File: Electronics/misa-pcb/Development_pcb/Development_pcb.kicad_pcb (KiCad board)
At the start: 2 copper layers, 100 x 100 mm, 25 parts, among them J1 Pan-Servo, J2 Tilt-Servo, J3 cam-power, J4 laser-power, J5 SPEAKER, J6 TFT_display, J7 lidar-TOF, J8 USB_C_IN, Q1 PN2222A, U1 ESP32-S3-DEVKITC-1-N8R8, U2 MP3-TF-16P

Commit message: Add new components and testing scripts for MISA PCB project
- Created MP3-TF-16P symbol library for KiCad with detailed properties.
- Added HTML redirect page for SnapEDA import guide.
- Implemented MISA_Camera_Only_Test.py for camera functionality testing with face detection.
- Developed TEST_1_PanTilt.ino for pan/tilt servo control with safety limits.
- Created TEST_2_DFPlayer.ino for standalone DFPlayer testing with serial control.
- Added TEST_3_Laser.ino for laser module testing with safety reminders.
- Implemented TEST_4_LiDAR.ino for TF-Luna LIDAR distance measurement.
- Developed TEST_5_TFT.ino for TFT screen testing with color fill and border checks.
- Added yolov8n.pt model file for object detection.
- Introduced Doctor and Human classes in Java with constructors and methods for specialization and name handling.
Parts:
- added C6: 100µF 16v, Capacitor_THT:CP_Radial_D5.0mm_P2.50mm, F.Cu at (254.0, 90.2)
- added G***: LOGO, LOGO, F.Cu at (255.3, 69.8)
- added G***: LOGO, LOGO, F.Cu at (266.1, 69.8)
- C1: renamed from C2; value 100nF -> 100nF 50v; footprint Capacitor_THT:C_Disc_D5.0mm_W2.5mm_P5.00mm -> Capacitor_THT:C_Disc_D5.0mm_W2.5mm_P2.50mm
- C2: renamed from C1; value 1000µF -> 1000µF 16v
- C3, C4: value 470µF -> 470µF 16v
- C5: value 100nF -> 100nF 50v; footprint Capacitor_THT:C_Disc_D5.0mm_W2.5mm_P5.00mm -> Capacitor_THT:C_Disc_D5.0mm_W2.5mm_P2.50mm
- D1: value SA5.0A -> SA6.0A
- F1: value Polyfuse -> MF-RG600; footprint Capacitor_THT:C_Disc_D5.0mm_W2.5mm_P5.00mm -> Fuse:Fuse_Bourns_MF-RG600
- J1, J2: footprint Connector_PinHeader_2.54mm:PinHeader_1x03_P2.54mm_Vertical -> Connector_JST:JST_XH_B3B-XH-A_1x03_P2.50mm_Vertical
- J7: footprint Connector_PinHeader_2.54mm:PinHeader_1x04_P2.54mm_Vertical -> Connector_JST:JST_XH_B4B-XH-A_1x04_P2.50mm_Vertical
- J8: footprint TerminalBlock_Phoenix:TerminalBlock_Phoenix_MKDS-3-2-5.08_1x02_P5.08mm_Horizontal -> TerminalBlock:TerminalBlock_Xinya_XY308-2.54-2P_1x02_P2.54mm_Horizontal
- R2: renamed from R4; value 1kΩ -> 220Ω
- moved D1 175.9 mm to (213.4, 148.6)
- moved C1 175.2 mm to (221.0, 148.6)
- moved C2 175.2 mm to (231.1, 148.6)
- moved C3 172.8 mm to (196.8, 115.6), turned to 90 degrees
- moved J2 167.7 mm to (208.3, 110.5), turned to -90 degrees
- moved C4 167.4 mm to (196.8, 102.9), turned to 90 degrees
- moved J1 167.1 mm to (208.3, 97.8), turned to -90 degrees
- moved D2 165.5 mm to (213.4, 121.9)
- moved C5 159.9 mm to (262.9, 90.2), turned to -90 degrees
- moved J4 159.6 mm to (271.8, 82.5)
- moved J6 159.6 mm to (210.8, 76.2)
- moved Q1 159.6 mm to (262.9, 80.0)
- moved R2 159.6 mm to (247.7, 81.3)
- moved U1 159.6 mm to (243.8, 71.1)
- moved G*** 159.0 mm to (259.1, 149.9)
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- renumbered R3 to R1
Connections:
- J1 pad 1: GND -> /PAN_PWM
- J1 pad 2: +5V -> GND
- J1 pad 3: /PAN_PWM -> +5V
- J2 pad 1: GND -> /TILT_PWM
- J2 pad 2: +5V -> GND
- J2 pad 3: /TILT_PWM -> +5V
- J6 pad 2: /TFT_SCK -> /TFT_CS
- J6 pad 3: /TFT_MOSI -> /TFT_DC
- J6 pad 4: /TFT_DC -> /TFT_RST
- J6 pad 5: /TFT_RST -> /TFT_SDA
- J6 pad 6: /TFT_CS -> /TFT_SCL
- J6 pad 7: GND -> +3V3
- J6 pad 8: +3V3 -> GND
- U1 pad J1_11: unconnected-(U1-GPIO18-PadJ1_11) -> /PAN_PWM
- U1 pad J1_15: /PAN_PWM -> unconnected-(U1-GPIO9-PadJ1_15)
- U1 pad J1_18: unconnected-(U1-GPIO12-PadJ1_18) -> /DF_RX
- U1 pad J1_19: /DF_RX -> /DF_TX
- U1 pad J1_20: /DF_TX -> /DF_BUSY
- U1 pad J1_4: /TFT_SCK -> /TFT_CS
- U1 pad J1_5: /TFT_MOSI -> /TFT_DC
- U1 pad J1_6: /TFT_DC -> /TFT_RST
- U1 pad J1_7: /TFT_RST -> /TFT_SDA
- U1 pad J1_8: /TFT_CS -> /TFT_SCL
- U2 pad P$16: unconnected-(U2-BUSY-PadP$16) -> /DF_BUSY
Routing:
- net /DF_BUSY: track 0.00 -> 97.2 mm
- net +5V: track 290.1 -> 325.4 mm
- net /TFT_SCL: track 0.00 -> 31.5 mm
- net /TFT_SDA: track 0.00 -> 26.4 mm
- net /TFT_CS: track 31.5 -> 11.2 mm
- net /TFT_MOSI: track 16.3 -> 0.00 mm
- net GND: track 13.5 -> 0.00 mm
- net /TFT_SCK: track 11.2 -> 0.00 mm
- net Net-(D2-K): track 11.2 -> 5.08 mm
- net /PAN_PWM: track 16.7 -> 10.7 mm
- net Net-(J8-Pin_2): track 12.8 -> 7.70 mm
- net /TFT_RST: track 26.4 -> 21.3 mm
- net /TFT_DC: track 21.3 -> 16.3 mm
- net +3V3: track 36.1 -> 31.5 mm
- net Net-(U2-RX): track 22.6 -> 26.8 mm
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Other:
- board text added: "+"
- board text added: "-"
- board text added: "Antena-Zone"

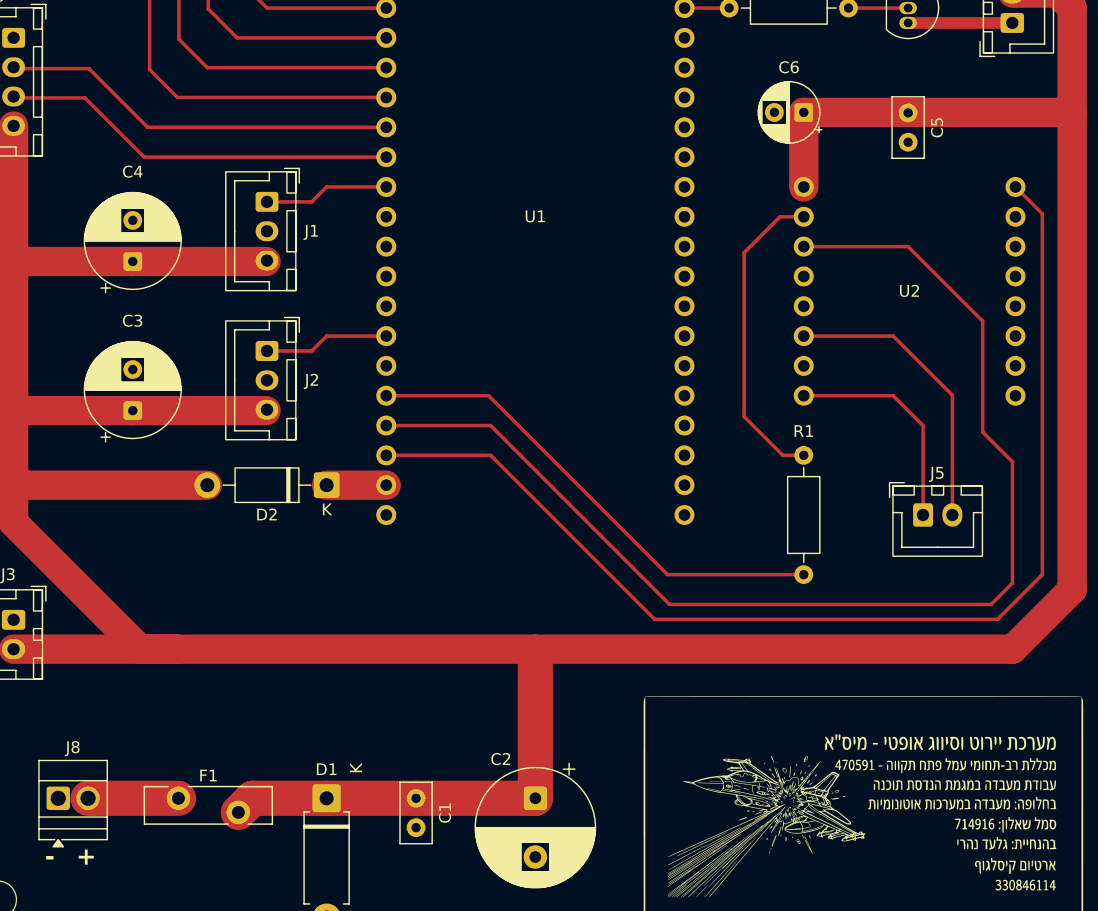
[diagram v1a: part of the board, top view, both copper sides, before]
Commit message: Add .DS_Store file to Python directory for macOS compatibility
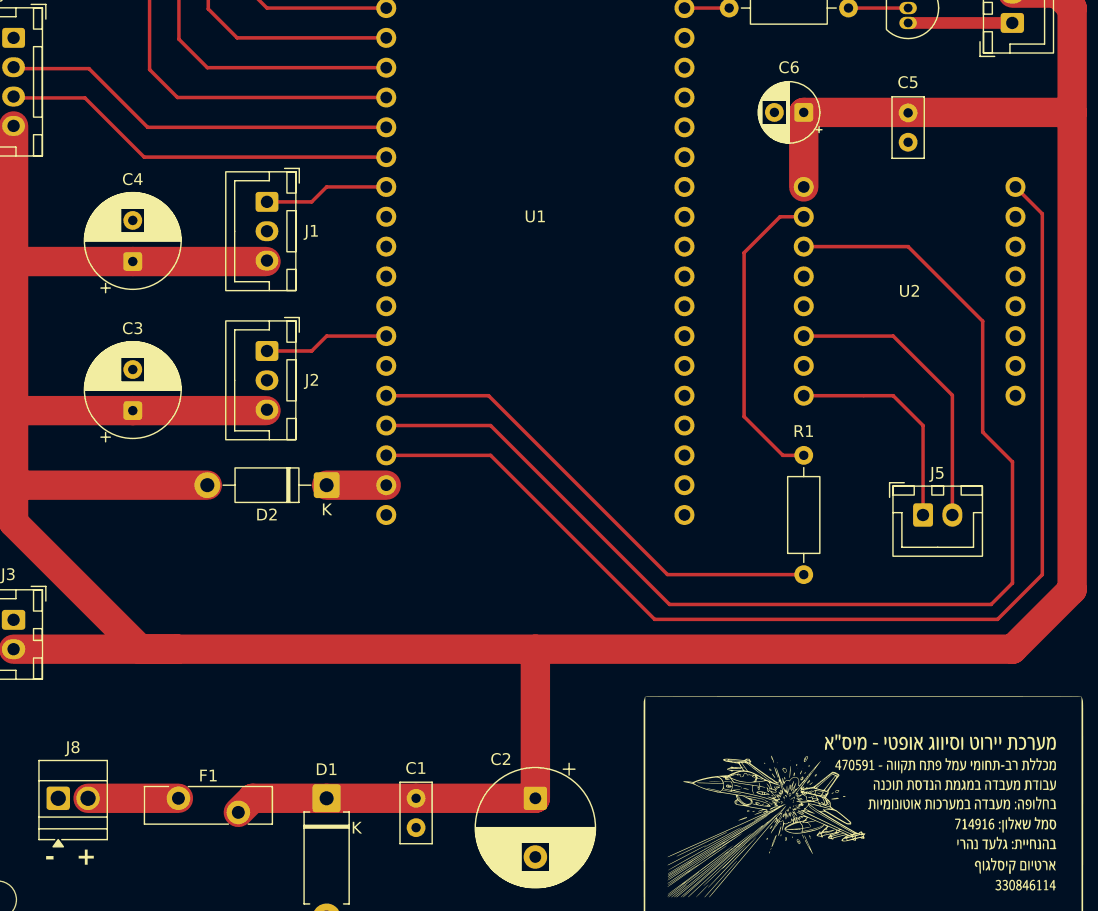
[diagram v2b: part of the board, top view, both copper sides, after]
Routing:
- net +5V: track 325.4 -> 326.8 mm
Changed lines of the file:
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@@
 		)
 		(fp_text user "K"
-			(at -2.54 -2.54 90)
+			(at 2.54 -2.54 180)
 			(layer "F.SilkS")
 			(effects
@@
 		(tags "C Disc series Radial pin pitch 2.50mm diameter 5mm width 2.5mm Capacitor")
 		(property "Reference" "C1"
-			(at 1.25 -2.5 270)
+			(at -2.54 0 0)
 			(layer "F.SilkS")
 			(effects
@@
 		)
 		(property "Value" "100nF 50v"
-			(at 1.25 2.5 270)
+			(at 5.08 0 0)
 			(layer "F.Fab")
 			(effects
@@
 		(tags "CP Radial series Radial pin pitch 3.50mm diameter 8mm height 12mm Electrolytic Capacitor")
 		(property "Reference" "C3"
-			(at 7.62 0 0)
+			(at 6.985 0 0)
 			(layer "F.SilkS")
 			(effects
@@
 		(tags "C Disc series Radial pin pitch 2.50mm diameter 5mm width 2.5mm Capacitor")
 		(property "Reference" "C5"
-			(at 1.25 -2.5 270)
+			(at -2.58 0 0)
 			(layer "F.SilkS")
 			(effects
@@
 		(tags "CP Radial series Radial pin pitch 3.50mm diameter 8mm height 12mm Electrolytic Capacitor")
 		(property "Reference" "C4"
-			(at 7.62 0 0)
+			(at 6.985 0 0)
 			(layer "F.SilkS")
 			(effects
@@
 		(start 220.98 148.59)
 		(end 231.14 148.59)
-		(width 3)
+		(width 2.5)
 		(layer "F.Cu")
 		(net "+5V")
@@
 		(start 207.04 148.59)
 		(end 205.84 149.79)
-		(width 3)
+		(width 2.5)
 		(layer "F.Cu")
 		(net "+5V")
@@
 	)
 	(segment
-		(start 271.78 135.89)
-		(end 231.14 135.89)
+		(start 200.66 135.89)
+		(end 271.78 135.89)
 		(width 2.5)
 		(layer "F.Cu")
@@
 	)
 	(segment
-		(start 213.36 148.59)
-		(end 220.98 148.59)
-		(width 3)
+		(start 231.14 148.59)
+		(end 231.14 135.89)
+		(width 2.5)
 		(layer "F.Cu")
 		(net "+5V")
 	)
 	(segment
-		(start 231.14 135.89)
-		(end 200.66 135.89)
+		(start 213.36 148.59)
+		(end 220.98 148.59)
 		(width 2.5)
 		(layer "F.Cu")
@@
 		(start 213.36 148.59)
 		(end 207.04 148.59)
-		(width 3)
+		(width 2.5)
 		(layer "F.Cu")
 		(net "+5V")
@@
 	)
 	(segment
-		(start 231.14 148.59)
-		(end 231.14 137.287)
-		(width 3)
-		(layer "F.Cu")
-		(net "+5V")
-	)
-	(segment
 		(start 196.85 102.87)
 		(end 208.2 102.87)
@@
 		(start 200.74 148.59)
 		(end 193.04 148.59)
-		(width 3)
+		(width 2.5)
 		(layer "F.Cu")
 		(net "Net-(J8-Pin_2)")

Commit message: Refactor code structure for improved readability and maintainability
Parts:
- added C10: 100µF 16v, Capacitor_THT:CP_Radial_D5.0mm_P2.50mm, F.Cu at (198.0, 135.9)
- added C11: 470µF 16v, Capacitor_THT:CP_Radial_D8.0mm_P3.50mm, F.Cu at (274.5, 80.0)
- added C12: 100nF 50v, Capacitor_THT:C_Disc_D5.0mm_W2.5mm_P2.50mm, F.Cu at (268.2, 80.0)
- added C13: 100nF 50v, Capacitor_THT:C_Disc_D5.0mm_W2.5mm_P2.50mm, F.Cu at (195.8, 66.0)
- added C14: 100µF 16v, Capacitor_THT:CP_Radial_D5.0mm_P2.50mm, F.Cu at (202.2, 68.5)
- added C7: 470µF 16v, Capacitor_THT:CP_Radial_D8.0mm_P3.50mm, F.Cu at (208.3, 121.9)
- added C8: 100nF 50v, Capacitor_THT:C_Disc_D5.0mm_W2.5mm_P2.50mm, F.Cu at (214.6, 124.4)
- added C9: 100nF 50v, Capacitor_THT:C_Disc_D5.0mm_W2.5mm_P2.50mm, F.Cu at (192.0, 135.9)
- C2: footprint Capacitor_THT:CP_Radial_D10.0mm_P5.00mm -> Capacitor_THT:CP_Radial_D12.5mm_P5.00mm
- R2: footprint Resistor_THT:R_Axial_DIN0207_L6.3mm_D2.5mm_P10.16mm_Horizontal -> Resistor_THT:R_Axial_DIN0207_L6.3mm_D2.5mm_P2.54mm_Vertical
- moved D2 11.4 mm to (201.9, 121.9)
- moved J4 9.79 mm to (262.0, 82.5)
- moved C6 9.45 mm to (263.2, 92.1), turned to 90 degrees
- moved C5 9.12 mm to (254.0, 92.1), turned to 90 degrees
- moved Q1 7.25 mm to (255.6, 80.0)
- moved R2 1.35 mm to (249.0, 81.3)
- moved C1 0.63 mm to (220.3, 148.6)
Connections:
- U1 pad J1_17: unconnected-(U1-GPIO11-PadJ1_17) -> /LASER_CTRL
- U1 pad J3_5: /LASER_CTRL -> unconnected-(U1-GPIO2-PadJ3_5)
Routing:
- net /LASER_CTRL: track 3.81 -> 81.9 mm
- net Net-(D2-K): track 5.08 -> 16.5 mm
- net +5V: track 326.8 -> 334.8 mm
- net +3V3: track 31.5 -> 38.1 mm
- net Net-(J4-Pin_1): track 8.87 -> 6.29 mm
- net /TFT_SCL: track 31.5 -> 30.0 mm
- net Net-(U2-RX): track 26.8 -> 25.7 mm
- net Net-(Q1-B): track 5.08 -> 4.10 mm
- net /DF_TX: track 101.6 -> 100.9 mm
- net /TFT_DC: track 16.3 -> 17.0 mm
- net /TFT_SDA: track 26.4 -> 25.7 mm
- net /TFT_CS: track 11.2 -> 12.0 mm

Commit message: Refactor code structure and remove redundant sections for improved readability and maintainability
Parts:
- added R3: 10kΩ, Resistor_THT:R_Axial_DIN0207_L6.3mm_D2.5mm_P2.54mm_Vertical, F.Cu at (248.9, 76.2)
- C10, C6: footprint Capacitor_THT:CP_Radial_D5.0mm_P2.50mm -> Capacitor_THT:CP_Radial_D6.3mm_P2.50mm
- R2: value 220Ω -> 100Ω
- moved C4 2.54 mm to (196.8, 100.3)
- moved C3 2.54 mm to (196.8, 113.0)
- moved C6 0.36 mm to (262.9, 92.1)
- moved C10 0.09 mm to (198.1, 135.9)
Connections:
- J1 pad 2: GND -> +5V
- J1 pad 3: +5V -> GND
- J2 pad 2: GND -> +5V
- J2 pad 3: +5V -> GND
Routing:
- net Net-(Q1-B): track 4.10 -> 9.92 mm
- net +5V: track 334.8 -> 336.8 mm
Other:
- board size 100 x 100 mm -> 100 x 99.5 mm
